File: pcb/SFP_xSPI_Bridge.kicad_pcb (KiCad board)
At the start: 2 copper layers, 46 parts, among them J1 SFP, J2 TC2050, J3 Conn_02x10_Odd_Even, U1 GW1N-6&9_QN48, Y1 OT322525MJBA4SL

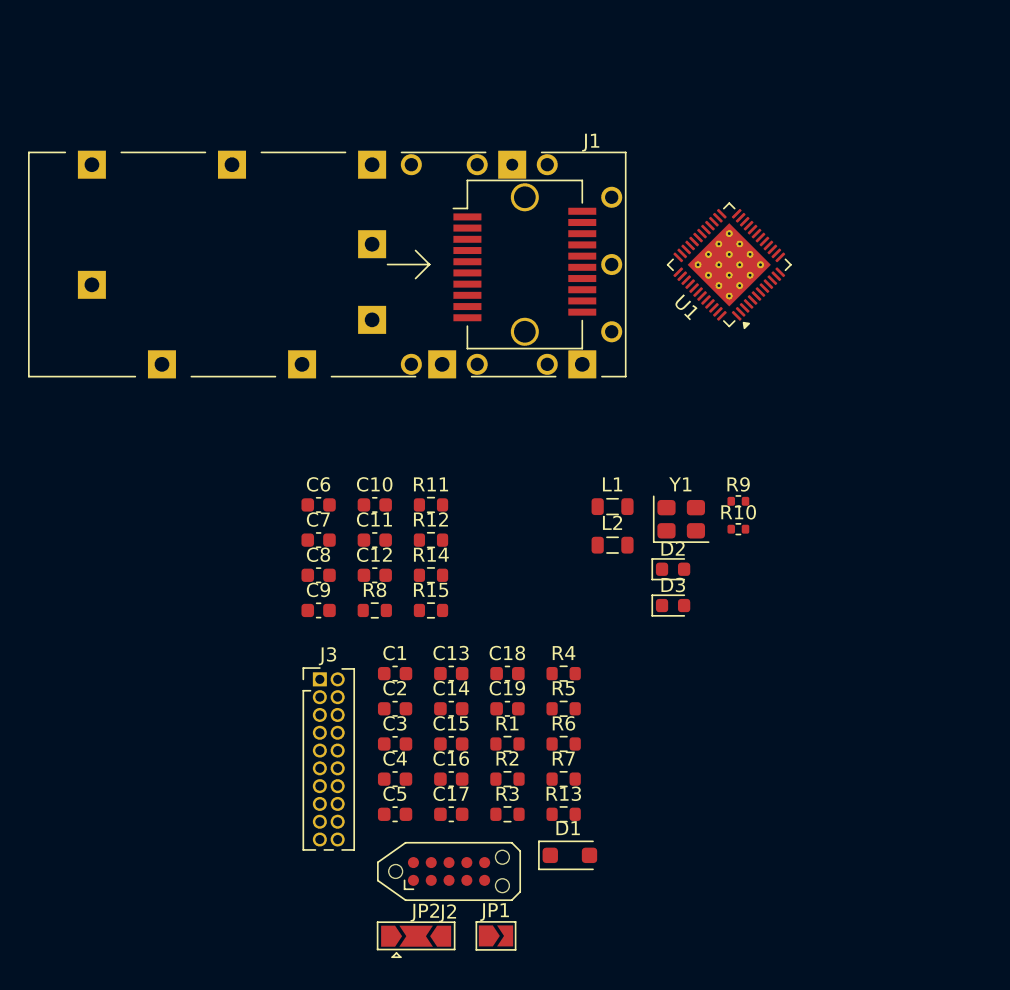
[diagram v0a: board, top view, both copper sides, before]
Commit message: pcb: rozmieszczenie i czesc routingu, odwrocona para RD, reguly i klasy sieci
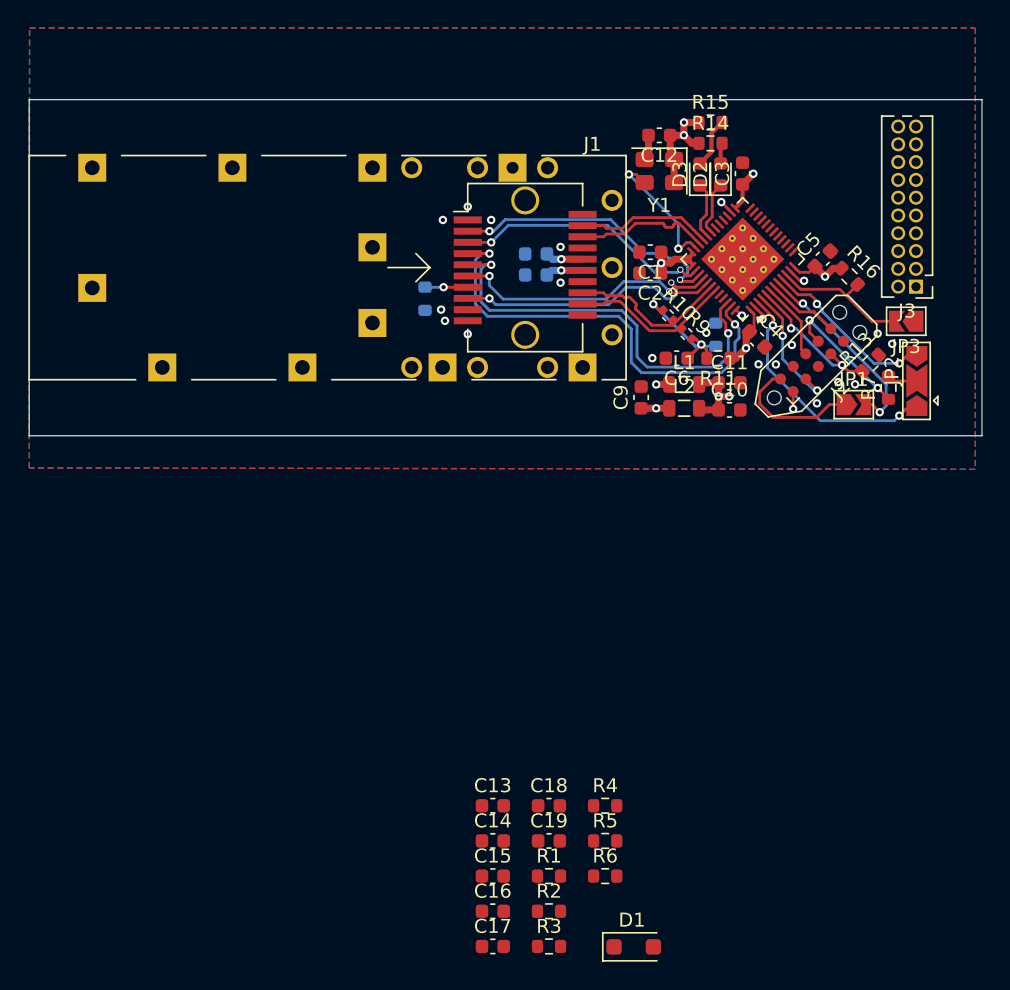
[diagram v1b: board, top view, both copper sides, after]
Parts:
- added JP3: SolderJumper_2_Open, Jumper:SolderJumper-2_P1.3mm_Open_TrianglePad1.0x1.5mm, F.Cu at (105.1, 34.6)
- added R16: 10k, Resistor_SMD:R_0603_1608Metric, F.Cu at (101.0, 31.4)
- C7, C8, R12, R8: moved to B.Cu
- moved JP2 53.4 mm to (105.8, 38.9), turned to 90 degrees
- moved J3 51.0 mm to (105.8, 32.2), turned to 180 degrees
- moved C5 50.0 mm to (99.1, 30.2), turned to 45 degrees
- moved C3 47.7 mm to (93.4, 24.1), turned to 90 degrees
- moved JP1 45.7 mm to (101.3, 40.6)
- moved J2 44.8 mm to (98.3, 37.4), turned to 45 degrees
- moved C4 40.7 mm to (94.4, 35.9), turned to -45 degrees
- moved R15 40.1 mm to (91.1, 20.4)
- moved R13 38.9 mm to (102.5, 37.6), turned to 45 degrees
- moved C12 37.4 mm to (87.5, 21.4), turned to 180 degrees
- moved R14 36.7 mm to (91.1, 21.9)
- moved R7 36.3 mm to (103.8, 39.4), turned to 90 degrees
- moved C2 36.0 mm to (86.8, 31.2), turned to 180 degrees
- moved C1 35.2 mm to (86.8, 29.7), turned to 180 degrees
- moved D3 30.8 mm to (90.3, 24.1), turned to 90 degrees
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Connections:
- R10 pad 2: /SFP/SFP_RD_N -> /SFP/SFP_RD_P
- R9 pad 1: /SFP/SFP_RD_P -> /SFP/SFP_RD_N
- U1 pad 10: unconnected-(U1D-IOL15A/GCLKT_6-Pad10) -> /EXT_IO/MODE_SEL
- U1 pad 42: /SFP/SFP_RD_N -> /SFP/SFP_RD_P
- U1 pad 43: /SFP/SFP_RD_P -> /SFP/SFP_RD_N
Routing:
- net /EXT_IO/SFP_SDA: track 0.00 -> 32.7 mm, vias 0 -> 2
- net +3V3: track 0.00 -> 31.1 mm, vias 0 -> 9
- net /EXT_IO/SFP_SCL: track 0.00 -> 30.4 mm, vias 0 -> 2
- net /SFP/SFP_TX_FAULT: track 0.00 -> 20.3 mm, vias 0 -> 2
- net /SFP/SFP_LOS: track 0.00 -> 19.8 mm, vias 0 -> 2
- net /SFP/SFP_MOD_ABS: track 0.00 -> 19.4 mm, vias 0 -> 2
- net /SFP/SFP_TX_DIS: track 0.00 -> 18.6 mm, vias 0 -> 2
- net Net-(J1-VccR): track 0.00 -> 18.3 mm, vias 0 -> 2
- net Net-(JP2-A): track 0.00 -> 17.8 mm, vias 0 -> 2
- net Net-(J1-VccT): track 0.00 -> 16.4 mm, vias 0 -> 2
- net Net-(JP1-B): track 0.00 -> 14.3 mm, vias 0 -> 2
- net Net-(JP2-B): track 0.00 -> 12.7 mm, vias 0 -> 2
- net /SFP/SFP_RD_N: track 0.00 -> 11.6 mm
- net /SFP/SFP_RD_P: track 0.00 -> 11.6 mm
- net /EXT_IO/TCK: track 0.00 -> 10.7 mm, vias 0 -> 2
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- added copper zone on F.Cu, net +3V3
- added copper zone on In2.Cu, net +3V3
- added copper zone on B.Cu, net GND
- added copper zone on F.Cu, net GND
- added copper zone on In1.Cu, net GND
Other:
- board outline added: 68 x 24 mm
- copper layers 2 -> 4
- rule pad_to_mask_clearance: 0 -> 0.05

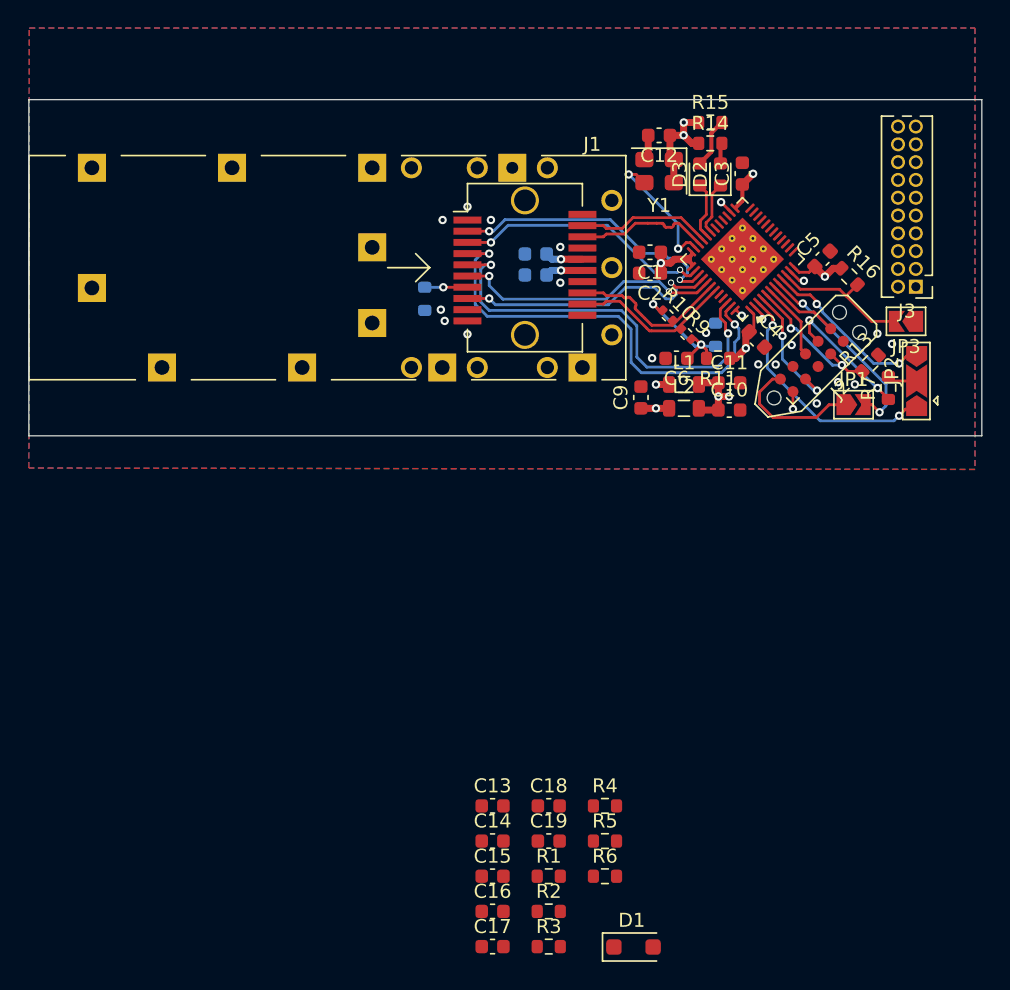
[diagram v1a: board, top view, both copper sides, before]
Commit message: pcb: routing par LVDS, zasilania i magistrali xSPI
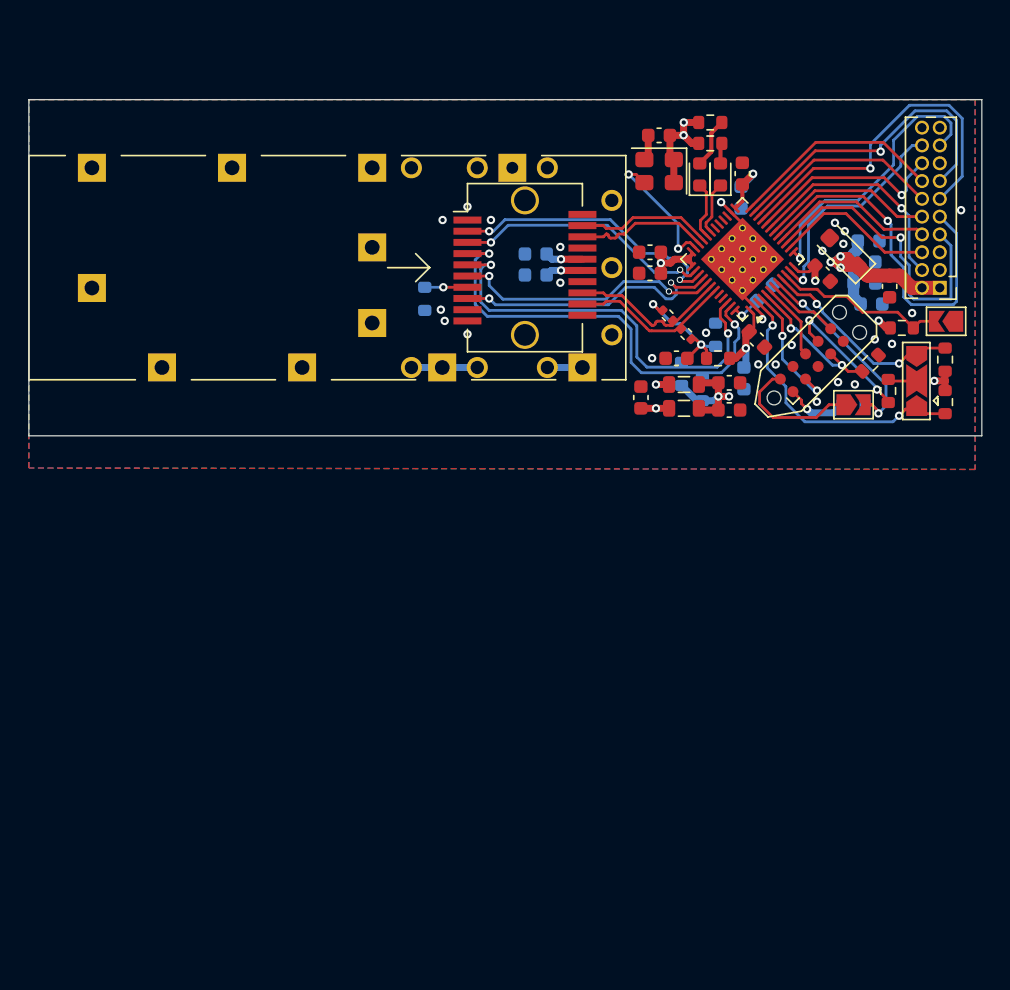
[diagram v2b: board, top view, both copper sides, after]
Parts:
- C14, C15, C16, C17, C18, C19, R2, R3, R4, R5: moved to B.Cu
- moved C17 54.3 mm to (102.1, 31.9), turned to 180 degrees
- moved C16 53.4 mm to (102.1, 30.4), turned to 180 degrees
- moved C15 52.7 mm to (102.4, 28.9), turned to 180 degrees
- moved D1 51.8 mm to (100.6, 29.7), turned to 135 degrees
- moved C19 47.9 mm to (93.3, 25.8), turned to -90 degrees
- moved C14 46.9 mm to (102.6, 33.4), turned to 180 degrees
- moved R2 46.8 mm to (95.0, 32.6), turned to 45 degrees
- moved C13 46.7 mm to (103.9, 32.1), turned to -90 degrees
- moved R6 44.1 mm to (107.9, 37.4), turned to 90 degrees
- moved R1 44.1 mm to (107.9, 40.4), turned to -90 degrees
- moved R3 41.3 mm to (90.5, 39.5), turned to 90 degrees
- moved R5 35.8 mm to (101.3, 40.6)
- moved C18 33.5 mm to (93.5, 38.7), turned to 90 degrees
- moved R4 31.3 mm to (89.0, 38.4), turned to 90 degrees
- moved R16 5.25 mm to (104.8, 35.1), turned to 0 degrees
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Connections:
- U1 pad 49: (no net) -> GND
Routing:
- net +3V3: track 31.1 -> 66.0 mm, vias 9 -> 14
- net /EXT_IO/XSPI_IO2: track 0.00 -> 26.3 mm, vias 0 -> 1
- net /EXT_IO/XSPI_IO4: track 0.00 -> 25.5 mm, vias 0 -> 1
- net /EXT_IO/XSPI_IO6: track 0.00 -> 22.9 mm, vias 0 -> 1
- net /EXT_IO/XSPI_IO0: track 0.00 -> 22.5 mm, vias 0 -> 1
- net /EXT_IO/HOST_IRQ_N: track 0.00 -> 20.2 mm, vias 0 -> 1
- net /EXT_IO/XSPI_SCLK: track 0.00 -> 16.4 mm, vias 0 -> 1
- net /EXT_IO/XSPI_IO7: track 0.00 -> 15.4 mm
- net /EXT_IO/HOST_RST_N: track 1.32 -> 16.2 mm
- net /EXT_IO/XSPI_IO5: track 0.00 -> 14.5 mm
- net /EXT_IO/XSPI_DQS: track 0.00 -> 14.5 mm, vias 0 -> 1
- net /EXT_IO/XSPI_IO3: track 0.00 -> 12.6 mm
- net /EXT_IO/XSPI_IO1: track 0.00 -> 12.1 mm
- net /EXT_IO/XSPI_CS_N: track 0.00 -> 11.6 mm
- net GND: track 4.07 -> 14.2 mm, vias 20 -> 26
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
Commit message: pcb: otwory montazowe, zakonczenie routingu rev. A
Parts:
- added H1: MountingHole_Pad, MountingHole:MountingHole_2.7mm_M2.5_DIN965_Pad, F.Cu at (95.8, 19.9)
- added H2: MountingHole_Pad, MountingHole:MountingHole_2.7mm_M2.5_DIN965_Pad, F.Cu at (45.5, 19.1)
- added H3: MountingHole_Pad, MountingHole:MountingHole_2.7mm_M2.5_DIN965_Pad, F.Cu at (45.5, 42.5)
- added H4: MountingHole_Pad, MountingHole:MountingHole_2.7mm_M2.5_DIN965_Pad, F.Cu at (79.5, 42.5)
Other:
- board size 68 x 24 mm -> 68 x 29.3 mm

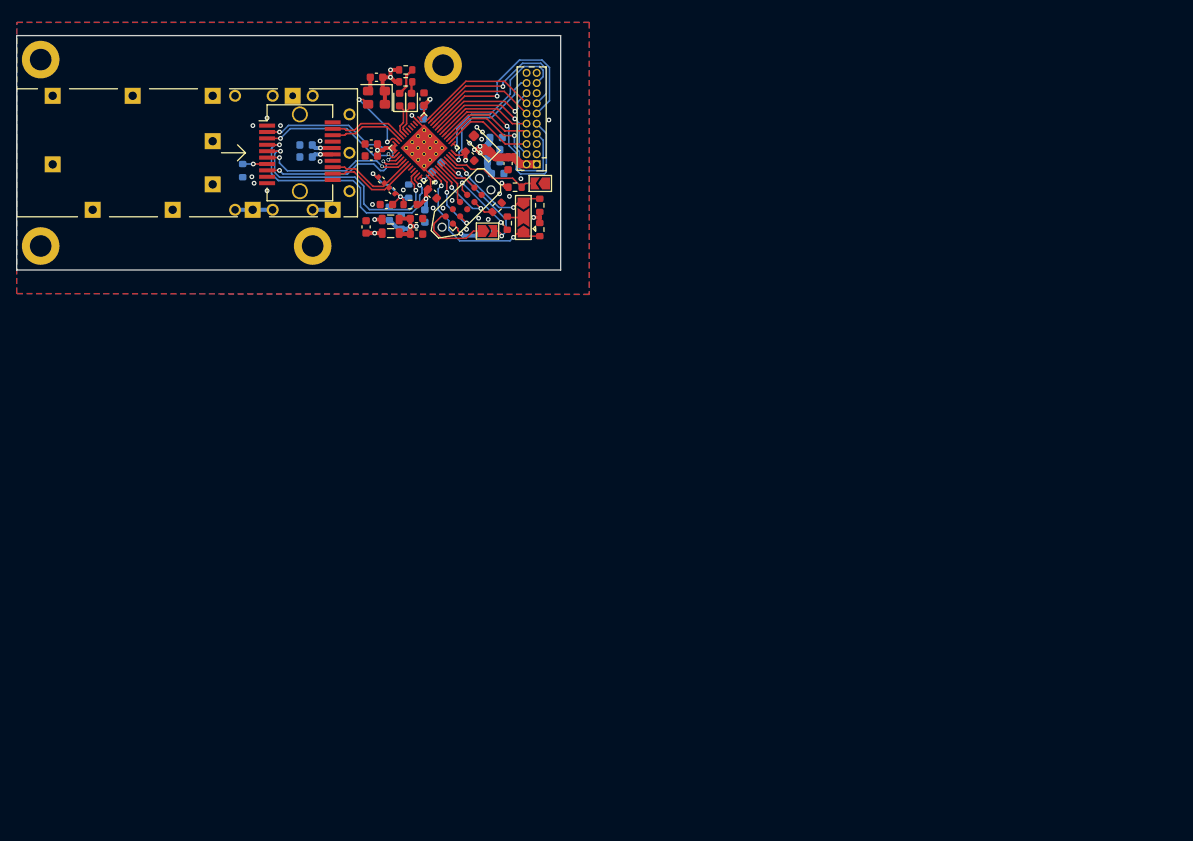
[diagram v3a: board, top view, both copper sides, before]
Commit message: pcb: rev. A - obrys, strefy, pull-up SFP_TX_DIS, via stitching, usuniete puste arkusze; pliki produkcyjne: gerbery (zip), PDF schematu i PCB, iBOM, rendery 3D
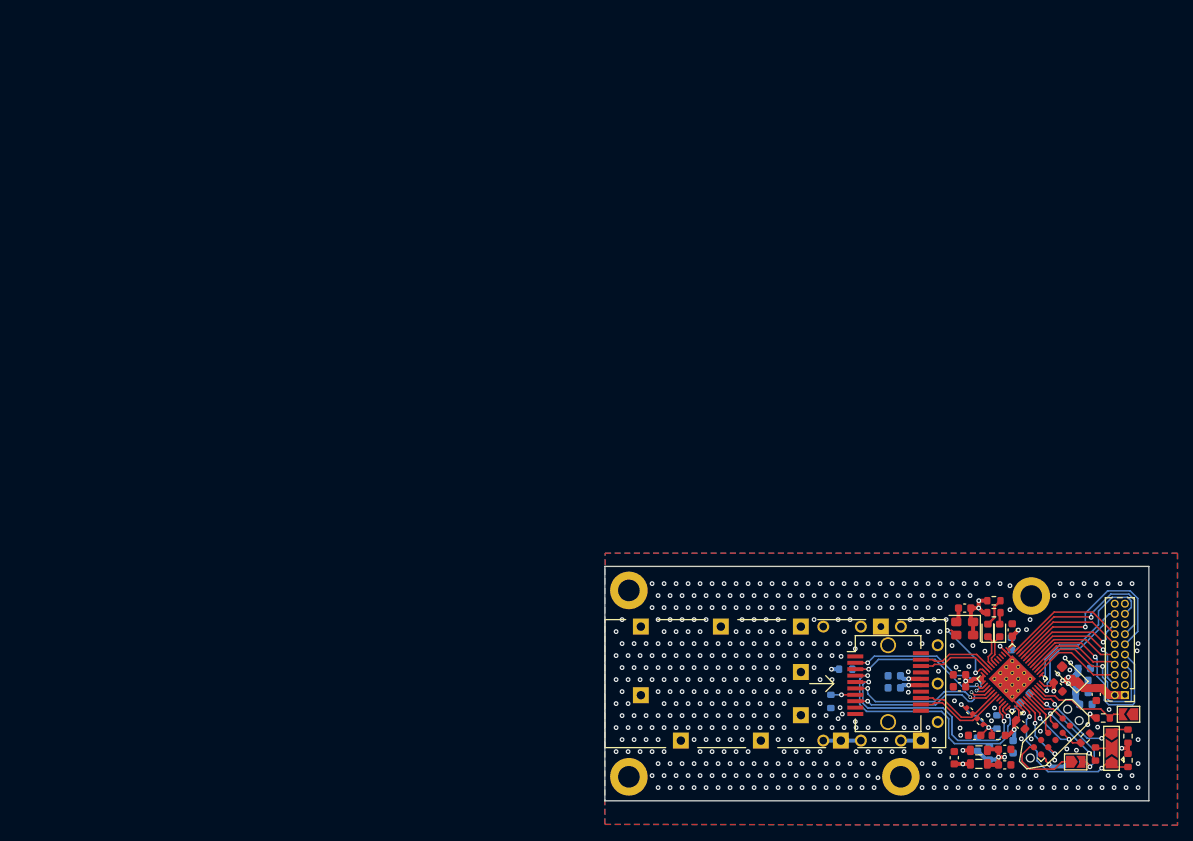
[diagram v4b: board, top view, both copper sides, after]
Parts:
- added R17: 4.7k, Resistor_SMD:R_0603_1608Metric, B.Cu at (146.1, 95.3)
- moved C10 99.0 mm to (166.0, 107.3)
- moved C14 99.0 mm to (176.1, 99.8)
- moved C15 99.0 mm to (175.9, 95.3)
- moved C16 99.0 mm to (175.6, 96.8)
- moved C17 99.0 mm to (175.6, 98.3)
- moved D2 99.0 mm to (165.4, 90.5)
- moved D3 99.0 mm to (163.9, 90.5)
- moved H2 99.0 mm to (119.0, 85.5)
- moved R10 99.0 mm to (161.6, 100.6)
- moved R13 99.0 mm to (176.0, 104.0)
- moved R14 99.0 mm to (164.6, 88.3)
- moved R8 99.0 mm to (144.3, 99.4)
- moved C1 99.0 mm to (160.3, 96.1)
- moved C12 99.0 mm to (161.0, 87.7)
- moved C13 99.0 mm to (177.4, 98.5)
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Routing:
- net /SFP/SFP_TX_DIS: track 18.6 -> 20.6 mm
- net +3V3: track 66.0 -> 66.9 mm, vias 14 -> 15
- net GND: vias 26 -> 437
